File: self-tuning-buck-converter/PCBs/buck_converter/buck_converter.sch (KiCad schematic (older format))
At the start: 31 parts, among them Q1 NMOS, U1 LT1999-50, U2 LM7322, U3 IR2125, U4 ESP32-DEVKITC-32D

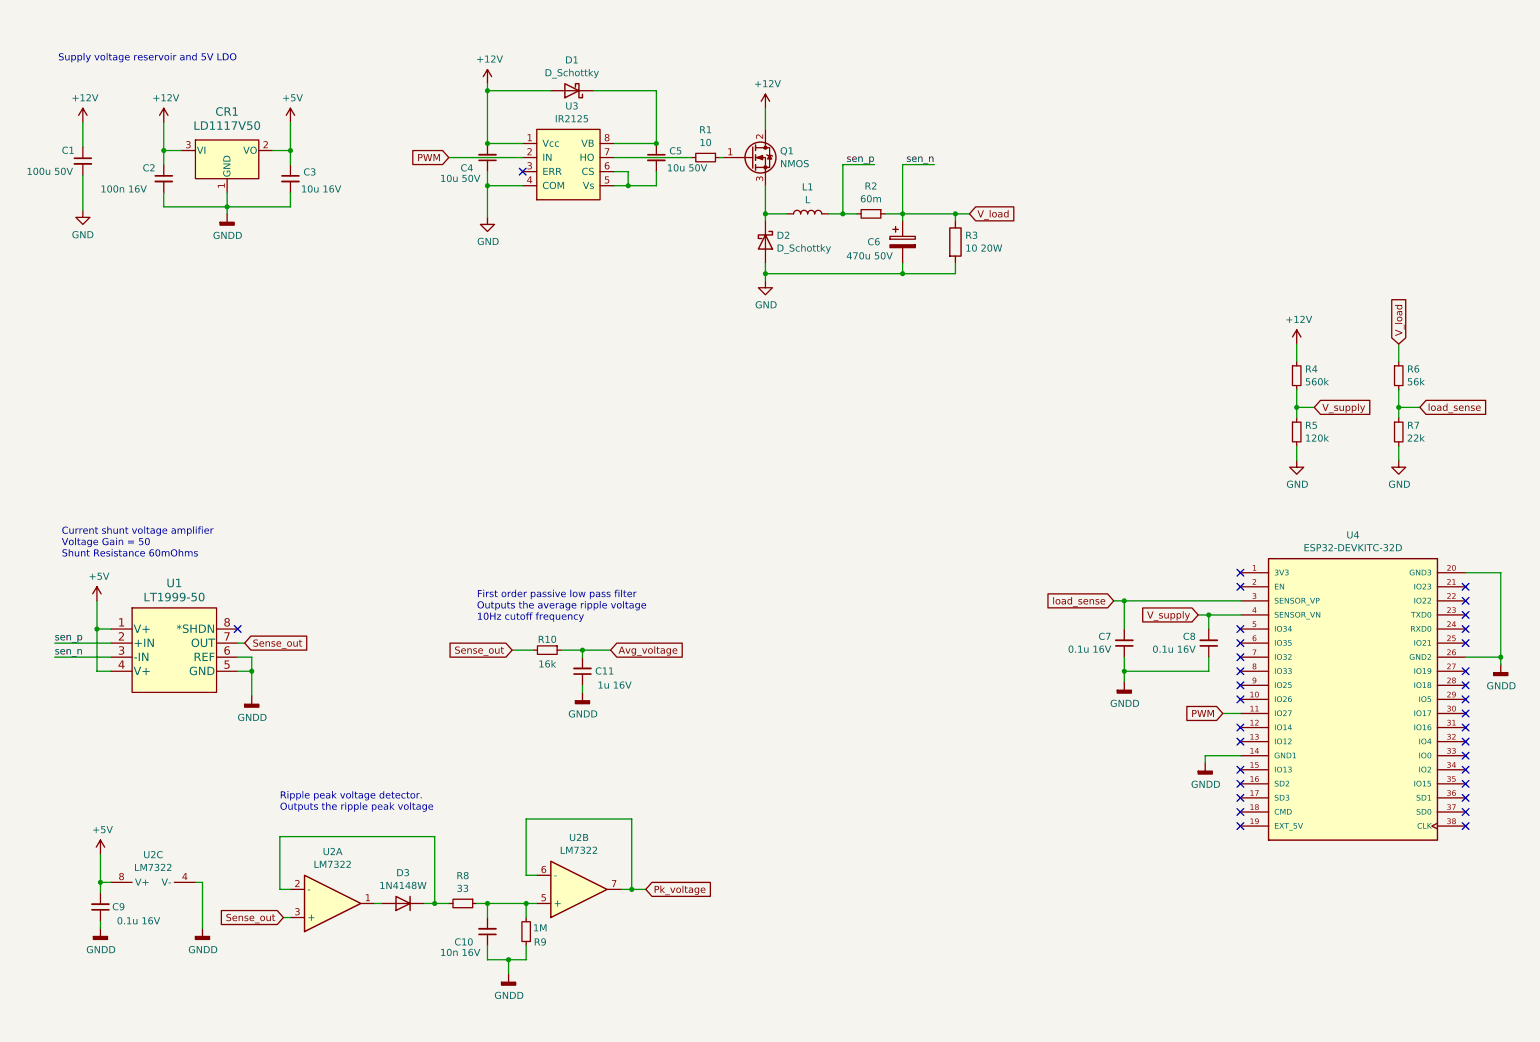
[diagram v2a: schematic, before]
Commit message: updated schematic with bypass capacitors, and added small filter caps to the ESP32's ADC input pins as recomended by the the datasheet
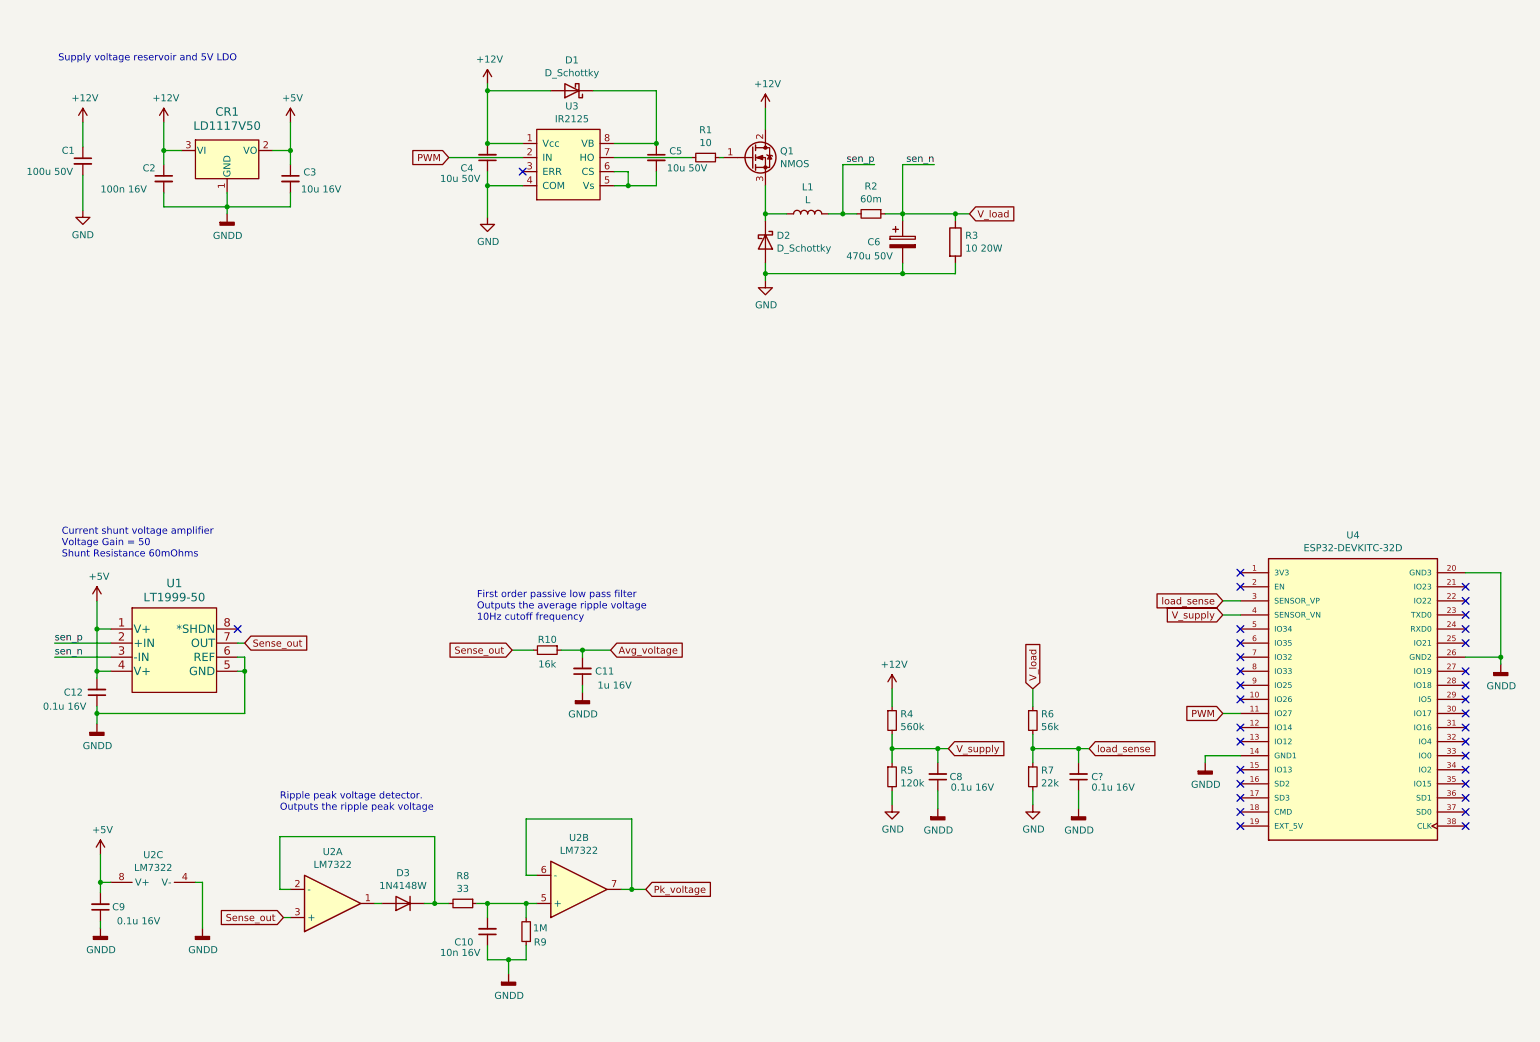
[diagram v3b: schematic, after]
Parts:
- removed C7: 0.1u 16V, symbol Device:C_Small
- added C12, C?: 0.1u 16V, symbol Device:C_Small
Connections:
- net +5V: now also C12.2
- net GNDD: now also C12.1, C?.1
- net load_sense: now also C?.2
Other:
- moved on the sheet: C8, R4, R5, R6, R7
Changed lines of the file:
@@
 NoConn ~ 9200 4600
 NoConn ~ 9200 6300
-Text GLabel 8900 4800 0    50   Input ~ 0
+Text GLabel 9075 4800 0    50   Input ~ 0
 V_supply
 NoConn ~ 9200 4900
@@
 L Device:R_Small R6
 U 1 1 6137AA0B
-P 10325 3100
-F 0 "R6" H 10384 3146 50  0000 L CNN
-F 1 "56k" H 10384 3055 50  0000 L CNN
-F 2 "" H 10325 3100 50  0001 C CNN
-F 3 "~" H 10325 3100 50  0001 C CNN
-	1    10325 3100
-	1    0    0    -1
-$EndComp
-Wire Wire Line
-	10325 2875 10325 3000
+P 7725 5550
+F 0 "R6" H 7784 5596 50  0000 L CNN
+F 1 "56k" H 7784 5505 50  0000 L CNN
+F 2 "" H 7725 5550 50  0001 C CNN
+F 3 "~" H 7725 5550 50  0001 C CNN
+	1    7725 5550
+	1    0    0    -1
+$EndComp
+Wire Wire Line
+	7725 5325 7725 5450
 $Comp
 L Device:R_Small R7
 U 1 1 6137C4E4
-P 10325 3500
-F 0 "R7" H 10384 3546 50  0000 L CNN
-F 1 "22k" H 10384 3455 50  0000 L CNN
-F 2 "" H 10325 3500 50  0001 C CNN
-F 3 "~" H 10325 3500 50  0001 C CNN
-	1    10325 3500
-	1    0    0    -1
-$EndComp
-Wire Wire Line
-	10325 3200 10325 3325
+P 7725 5950
+F 0 "R7" H 7784 5996 50  0000 L CNN
+F 1 "22k" H 7784 5905 50  0000 L CNN
+F 2 "" H 7725 5950 50  0001 C CNN
+F 3 "~" H 7725 5950 50  0001 C CNN
+	1    7725 5950
+	1    0    0    -1
+$EndComp
 $Comp
 L power:GND #PWR0105
 U 1 1 6137CD28
-P 10325 3700
-F 0 "#PWR0105" H 10325 3450 50  0001 C CNN
-F 1 "GND" H 10330 3527 50  0000 C CNN
-F 2 "" H 10325 3700 50  0001 C CNN
-F 3 "" H 10325 3700 50  0001 C CNN
-	1    10325 3700
-	1    0    0    -1
-$EndComp
-Wire Wire Line
-	10325 3600 10325 3700
+P 7725 6150
+F 0 "#PWR0105" H 7725 5900 50  0001 C CNN
+F 1 "GND" H 7730 5977 50  0000 C CNN
+F 2 "" H 7725 6150 50  0001 C CNN
+F 3 "" H 7725 6150 50  0001 C CNN
+	1    7725 6150
+	1    0    0    -1
+$EndComp
 $Comp
 L Device:R_Small R4
 U 1 1 6137E635
-P 9600 3100
-F 0 "R4" H 9659 3146 50  0000 L CNN
-F 1 "560k" H 9659 3055 50  0000 L CNN
-F 2 "" H 9600 3100 50  0001 C CNN
-F 3 "~" H 9600 3100 50  0001 C CNN
-	1    9600 3100
-	1    0    0    -1
-$EndComp
-Wire Wire Line
-	9600 2875 9600 3000
-$Comp
-L Device:R_Small R5
-U 1 1 6137E641
-P 9600 3500
-F 0 "R5" H 9659 3546 50  0000 L CNN
-F 1 "120k" H 9659 3455 50  0000 L CNN
-F 2 "" H 9600 3500 50  0001 C CNN
-F 3 "~" H 9600 3500 50  0001 C CNN
-	1    9600 3500
-	1    0    0    -1
-$EndComp
-Wire Wire Line
-	9600 3200 9600 3325
+P 6725 5550
+F 0 "R4" H 6784 5596 50  0000 L CNN
+F 1 "560k" H 6784 5505 50  0000 L CNN
+F 2 "" H 6725 5550 50  0001 C CNN
+F 3 "~" H 6725 5550 50  0001 C CNN
+	1    6725 5550
+	1    0    0    -1
+$EndComp
+Wire Wire Line
+	6725 5325 6725 5450
+Wire Wire Line
+	6725 5650 6725 5750
 $Comp
 L power:GND #PWR0106
 U 1 1 6137E64C
-P 9600 3700
-F 0 "#PWR0106" H 9600 3450 50  0001 C CNN
-F 1 "GND" H 9605 3527 50  0000 C CNN
-F 2 "" H 9600 3700 50  0001 C CNN
-F 3 "" H 9600 3700 50  0001 C CNN
-	1    9600 3700
-	1    0    0    -1
-$EndComp
-Wire Wire Line
-	9600 3600 9600 3700
+P 6725 6150
+F 0 "#PWR0106" H 6725 5900 50  0001 C CNN
+F 1 "GND" H 6730 5977 50  0000 C CNN
+F 2 "" H 6725 6150 50  0001 C CNN
+F 3 "" H 6725 6150 50  0001 C CNN
+	1    6725 6150
+	1    0    0    -1
+$EndComp
 $Comp
 L power:+12V #PWR0107
 U 1 1 6137FB09
-P 9600 2875
-F 0 "#PWR0107" H 9600 2725 50  0001 C CNN
-F 1 "+12V" H 9615 3048 50  0000 C CNN
-F 2 "" H 9600 2875 50  0001 C CNN
-F 3 "" H 9600 2875 50  0001 C CNN
-	1    9600 2875
-	1    0    0    -1
-$EndComp
-Text GLabel 9725 3325 2    50   Input ~ 0
+P 6725 5325
+F 0 "#PWR0107" H 6725 5175 50  0001 C CNN
+F 1 "+12V" H 6740 5498 50  0000 C CNN
+F 2 "" H 6725 5325 50  0001 C CNN
+F 3 "" H 6725 5325 50  0001 C CNN
+	1    6725 5325
+	1    0    0    -1
+$EndComp
+Text GLabel 7125 5750 2    50   Input ~ 0
 V_supply
 Wire Wire Line
-	9725 3325 9600 3325
-Connection ~ 9600 3325
-Wire Wire Line
-	9600 3325 9600 3400
-Wire Wire Line
-	8900 4800 8975 4800
+	7125 5750 7050 5750
+Connection ~ 6725 5750
+Wire Wire Line
+	6725 5750 6725 5850
 $Comp
 L Device:C_Small C8
 U 1 1 61384302
-P 8975 5000
-F 0 "C8" H 8883 4954 50  0000 R CNN
-F 1 "0.1u 16V" H 8883 5045 50  0000 R CNN
-F 2 "" H 8975 5000 50  0001 C CNN
-F 3 "~" H 8975 5000 50  0001 C CNN
-	1    8975 5000
+P 7050 5950
+F 0 "C8" H 7225 5950 50  0000 R CNN
+F 1 "0.1u 16V" H 7450 6025 50  0000 R CNN
+F 2 "" H 7050 5950 50  0001 C CNN
+F 3 "~" H 7050 5950 50  0001 C CNN
+	1    7050 5950
 	1    0    0    1
 $EndComp
@@
 L power:GNDD #PWR0108
 U 1 1 61385013
-P 8375 5275
-F 0 "#PWR0108" H 8375 5025 50  0001 C CNN
-F 1 "GNDD" H 8379 5120 50  0000 C CNN
-F 2 "" H 8375 5275 50  0001 C CNN
-F 3 "" H 8375 5275 50  0001 C CNN
-	1    8375 5275
-	1    0    0    -1
-$EndComp
-Wire Wire Line
-	8975 4900 8975 4800
-Connection ~ 8975 4800
-Wire Wire Line
-	8975 4800 9200 4800
-$Comp
-L Device:C_Small C7
-U 1 1 613883ED
-P 8375 5000
-F 0 "C7" H 8283 4954 50  0000 R CNN
-F 1 "0.1u 16V" H 8283 5045 50  0000 R CNN
-F 2 "" H 8375 5000 50  0001 C CNN
-F 3 "~" H 8375 5000 50  0001 C CNN
-	1    8375 5000
-	1    0    0    1
-$EndComp
-Wire Wire Line
-	8375 4700 9200 4700
-Wire Wire Line
-	8375 4700 8375 4900
-Text GLabel 10475 3325 2    50   Input ~ 0
+P 8050 6175
+F 0 "#PWR0108" H 8050 5925 50  0001 C CNN
+F 1 "GNDD" H 8054 6020 50  0000 C CNN
+F 2 "" H 8050 6175 50  0001 C CNN
+F 3 "" H 8050 6175 50  0001 C CNN
+	1    8050 6175
+	1    0    0    -1
+$EndComp
+Text GLabel 8125 5750 2    50   Input ~ 0
 load_sense
-Wire Wire Line
-	10475 3325 10325 3325
-Connection ~ 10325 3325
-Wire Wire Line
-	10325 3325 10325 3400
-Text GLabel 8300 4700 0    50   Input ~ 0
+Text GLabel 9075 4700 0    50   Input ~ 0
 load_sense
-Wire Wire Line
-	8300 4700 8375 4700
-Connection ~ 8375 4700
 Wire Wire Line
 	5825 2300 5825 2375
@@
 NoConn ~ 2075 4900
 Wire Wire Line
-	2075 5200 2175 5200
-Wire Wire Line
-	2075 5100 2175 5100
-Wire Wire Line
-	2175 5100 2175 5200
-Connection ~ 2175 5200
+	2075 5200 2125 5200
+Wire Wire Line
+	2075 5100 2125 5100
+Wire Wire Line
+	2125 5100 2125 5200
+Connection ~ 2125 5200
 Wire Wire Line
 	2075 5000 2125 5000
@@
 L power:GNDD #PWR06
 U 1 1 6152F858
-P 2175 5375
-F 0 "#PWR06" H 2175 5125 50  0001 C CNN
-F 1 "GNDD" H 2179 5220 50  0000 C CNN
-F 2 "" H 2175 5375 50  0001 C CNN
-F 3 "" H 2175 5375 50  0001 C CNN
-	1    2175 5375
-	1    0    0    -1
-$EndComp
-Wire Wire Line
-	2175 5200 2175 5375
+P 1075 5575
+F 0 "#PWR06" H 1075 5325 50  0001 C CNN
+F 1 "GNDD" H 1079 5420 50  0000 C CNN
+F 2 "" H 1075 5575 50  0001 C CNN
+F 3 "" H 1075 5575 50  0001 C CNN
+	1    1075 5575
+	1    0    0    -1
+$EndComp
 Wire Wire Line
 	1175 5000 775  5000
@@
 Wire Wire Line
 	6375 1600 6600 1600
-Wire Wire Line
-	8975 5100 8975 5200
-Wire Wire Line
-	8375 5200 8975 5200
 $Comp
 L LD1117V50:LD1117V50 CR1
@@
 Wire Wire Line
 	2000 1900 2450 1900
-Wire Wire Line
-	8375 5100 8375 5200
-Connection ~ 8375 5200
-Wire Wire Line
-	8375 5200 8375 5275
 $Comp
 L power:GNDD #PWR05
@@
 Wire Wire Line
 	1825 6700 1825 7025
-Text GLabel 10325 2875 1    50   Input ~ 0
+Text GLabel 7725 5325 1    50   Input ~ 0
 V_load
 $Comp
@@
 Text Notes 800  875  0    50   ~ 0
 Supply voltage reservoir and 5V LDO
+$Comp
+L Device:C_Small C12
+U 1 1 614BE6E3
+P 1075 5350
+F 0 "C12" H 975 5350 50  0000 R CNN
+F 1 "0.1u 16V" H 1000 5450 50  0000 R CNN
+F 2 "" H 1075 5350 50  0001 C CNN
+F 3 "~" H 1075 5350 50  0001 C CNN
+	1    1075 5350
+	1    0    0    1
+$EndComp
+Wire Wire Line
+	1075 5250 1075 5200
+Connection ~ 1075 5200
+Wire Wire Line
+	1075 5450 1075 5500
+Wire Wire Line
+	2125 5200 2125 5500
+Wire Wire Line
+	1075 5575 1075 5500
+Connection ~ 1075 5500
+Wire Wire Line
+	1075 5500 2125 5500
+Wire Wire Line
+	7050 6175 7050 6050
+Wire Wire Line
+	7050 5850 7050 5750
+Connection ~ 7050 5750
+Wire Wire Line
+	7050 5750 6725 5750
+$Comp
+L Device:R_Small R5
+U 1 1 6137E641
+P 6725 5950
+F 0 "R5" H 6784 5996 50  0000 L CNN
+F 1 "120k" H 6784 5905 50  0000 L CNN
+F 2 "" H 6725 5950 50  0001 C CNN
+F 3 "~" H 6725 5950 50  0001 C CNN
+	1    6725 5950
+	1    0    0    -1
+$EndComp
+Wire Wire Line
+	8125 5750 8050 5750
+$Comp
+L Device:C_Small C?
+U 1 1 615661DB
+P 8050 5950
+F 0 "C?" H 8225 5950 50  0000 R CNN
+F 1 "0.1u 16V" H 8450 6025 50  0000 R CNN
+F 2 "" H 8050 5950 50  0001 C CNN
+F 3 "~" H 8050 5950 50  0001 C CNN
+	1    8050 5950
+	1    0    0    1
+$EndComp
+Wire Wire Line
+	8050 5850 8050 5750
+Wire Wire Line
+	7725 5650 7725 5750
+Wire Wire Line
+	8050 5750 7725 5750
+Connection ~ 8050 5750
+Connection ~ 7725 5750
+Wire Wire Line
+	7725 5750 7725 5850
+Wire Wire Line
+	9075 4800 9200 4800
+Wire Wire Line
+	6725 6050 6725 6150
+Wire Wire Line
+	9075 4700 9200 4700
+$Comp
+L power:GNDD #PWR?
+U 1 1 615943DC
+P 7050 6175
+F 0 "#PWR?" H 7050 5925 50  0001 C CNN
+F 1 "GNDD" H 7054 6020 50  0000 C CNN
+F 2 "" H 7050 6175 50  0001 C CNN
+F 3 "" H 7050 6175 50  0001 C CNN
+	1    7050 6175
+	1    0    0    -1
+$EndComp
+Wire Wire Line
+	7725 6050 7725 6150
+Wire Wire Line
+	8050 6050 8050 6175
 $EndSCHEMATC

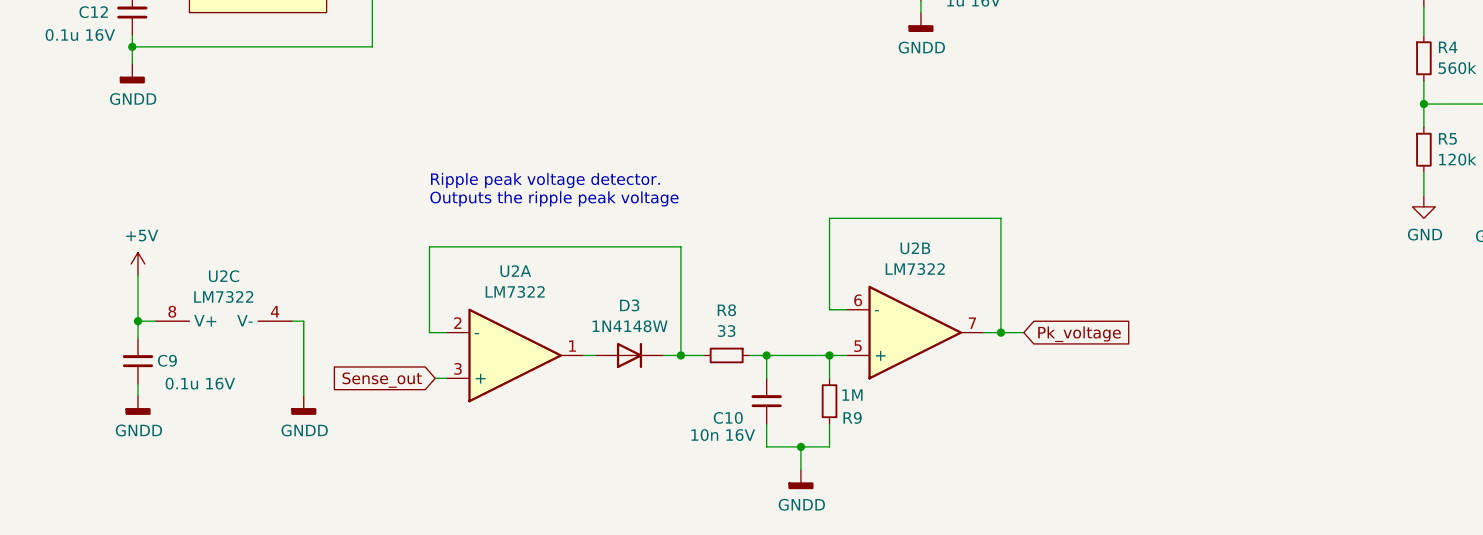
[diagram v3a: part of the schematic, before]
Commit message: updated the design of the peak detectror such that is imposes thepeaks on VCC/2. This voltage will vary as VCC shifts, but the differential ADC can be used to take accurate peak readings regardless, as it will reject the common mode voltage
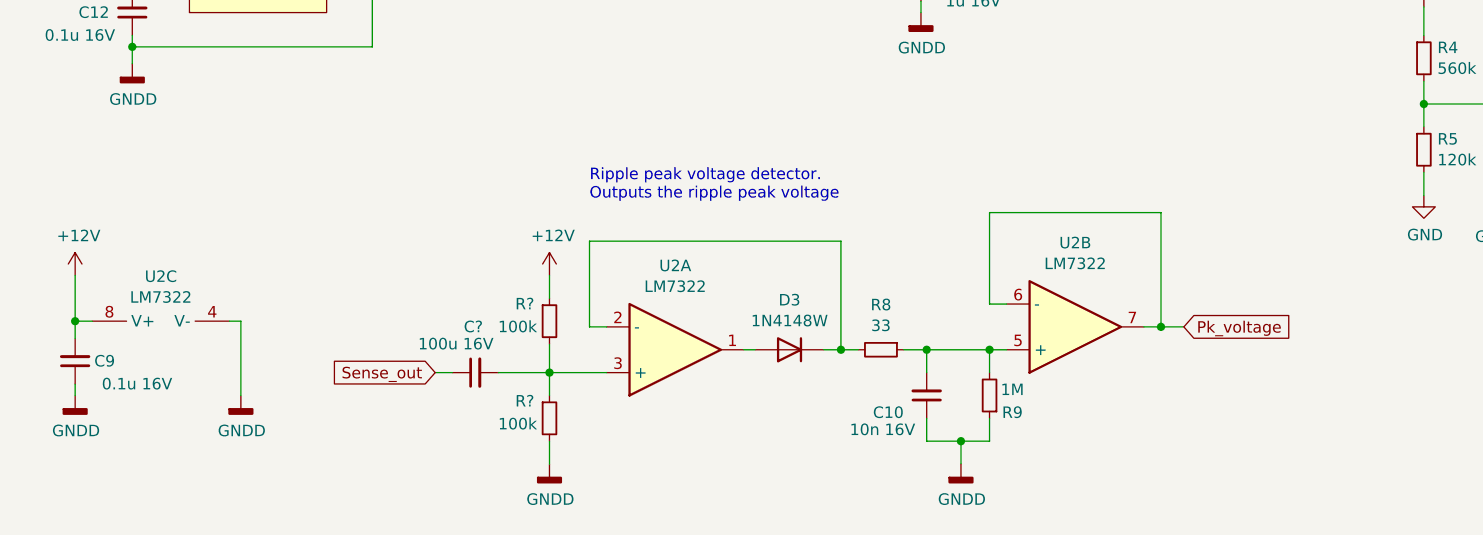
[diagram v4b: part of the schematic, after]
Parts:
- added C?: 100u 16V, symbol Device:C_Small
- added R? (x2): 100k, symbol Device:R_Small
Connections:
- net +12V: now also C9.2, U2.8 (V+), R?.1
- net +5V: no longer C9.2, U2.8 (V+)
- net GNDD: now also R?.2
- net Sense_out: now also C?.1; no longer U2.3 (+)
- new net: C?.2, R?.1, R?.2, U2.3 (+)
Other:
- moved on the sheet: C10, C9, D3, R8, R9, U2A, U2B, U2C
